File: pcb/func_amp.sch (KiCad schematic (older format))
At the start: 17 parts

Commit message: init pcb layout and gerber
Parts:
- removed J?: PWR, symbol Connector_Generic:Conn_01x02
- added C1: 0.33u, Capacitor_THT:CP_Radial_D5.0mm_P2.50mm, symbol Device:CP
- added C12: 2.2n, Capacitor_THT:C_Rect_L7.0mm_W3.5mm_P5.00mm, symbol Device:C
- added C2: 2.2u, Capacitor_THT:CP_Radial_D5.0mm_P2.50mm, symbol Device:CP
- added C3: 0.1u, Capacitor_THT:CP_Radial_D5.0mm_P2.50mm, symbol Device:CP
- added C4: 1u, Capacitor_THT:CP_Radial_D5.0mm_P2.50mm, symbol Device:CP
- added D1, D2: 1N4001, Diode_THT:D_DO-41_SOD81_P10.16mm_Horizontal, symbol Diode:1N4001
- added J1: PWR, TerminalBlock_Phoenix:TerminalBlock_Phoenix_MKDS-1,5-3-5.08_1x03_P5.08mm_Horizontal, symbol Connector_Generic:Conn_01x03
- added R5: 3R2, Resistor_THT:R_Axial_DIN0207_L6.3mm_D2.5mm_P10.16mm_Horizontal, symbol Device:R
- added R6: 50R, Resistor_THT:R_Axial_DIN0207_L6.3mm_D2.5mm_P10.16mm_Horizontal, symbol Device:R
- added U1: L7815, Package_TO_SOT_THT:TO-220-3_Vertical, symbol Regulator_Linear:L7815
- added U2: L7915, Package_TO_SOT_THT:TO-220-3_Vertical, symbol Regulator_Linear:L7915
- C10, C9: renamed from C?; footprint (none) -> Capacitor_THT:C_Rect_L7.0mm_W3.5mm_P5.00mm
- C11: renamed from C?; footprint (none) -> Capacitor_THT:C_Rect_L10.3mm_W5.7mm_P7.50mm_MKS4
- C5, C6: renamed from C?; footprint (none) -> Capacitor_THT:CP_Radial_D5.0mm_P2.50mm
- C7, C8: renamed from C?; footprint (none) -> Capacitor_THT:CP_Radial_D6.3mm_P2.50mm
- J2: renamed from J?; footprint (none) -> Connector_Coaxial:BNC_TEConnectivity_1478204_Vertical
- J3: renamed from J?; footprint (none) -> TerminalBlock_Phoenix:TerminalBlock_Phoenix_MKDS-1,5-2-5.08_1x02_P5.08mm_Horizontal
- R1, R3: renamed from R?; footprint (none) -> Resistor_THT:R_Axial_DIN0207_L6.3mm_D2.5mm_P10.16mm_Horizontal
- R2: renamed from R?; value 680 -> 680R; footprint (none) -> Resistor_THT:R_Axial_DIN0207_L6.3mm_D2.5mm_P10.16mm_Horizontal
- R4: renamed from R?; value 1 -> 1R; footprint (none) -> Resistor_THT:R_Axial_DIN0207_L6.3mm_D2.5mm_P10.16mm_Horizontal
- gave numbers to parts that had none: 3
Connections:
- net labels added: +15V, +V, -15V, -V
- net labels removed: +12V, -12V
- wire segments 49 -> 87

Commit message: update with available component value
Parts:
- R5: value 3R2 -> 4R7
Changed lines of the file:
@@
 P 5600 3850
 F 0 "R5" V 5680 3850 50  0000 C CNN
-F 1 "3R2" V 5600 3850 50  0000 C CNN
+F 1 "4R7" V 5600 3850 50  0000 C CNN
 F 2 "Resistor_THT:R_Axial_DIN0207_L6.3mm_D2.5mm_P10.16mm_Horizontal" V 5530 3850 50  0001 C CNN
 F 3 "~" H 5600 3850 50  0001 C CNN

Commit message: update schema
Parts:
- removed C12: 2.2n, Capacitor_THT:C_Rect_L7.0mm_W3.5mm_P5.00mm, symbol Device:C
- removed D1, D2: 1N4001, Diode_THT:D_DO-41_SOD81_P10.16mm_Horizontal, symbol Diode:1N4001
- removed J1: PWR, TerminalBlock_Phoenix:TerminalBlock_Phoenix_MKDS-1,5-3-5.08_1x03_P5.08mm_Horizontal, symbol Connector_Generic:Conn_01x03
- removed R5: 4R7, Resistor_THT:R_Axial_DIN0207_L6.3mm_D2.5mm_P10.16mm_Horizontal, symbol Device:R
- removed U1: L7815, Package_TO_SOT_THT:TO-220-3_Vertical, symbol Regulator_Linear:L7815
- removed U2: L7915, Package_TO_SOT_THT:TO-220-3_Vertical, symbol Regulator_Linear:L7915
- added C19: 220pF, symbol Device:C
- added D1: KBP10G, Diode_THT:Diode_Bridge_Vishay_KBPM, symbol Device:D_Bridge_+AA-
- added NT1: Net-Tie_3_Tee, NetTie:NetTie-3_SMD_Pad2.0mm, symbol Device:Net-Tie_3_Tee
- added P1: AC-01B, TerminalBlock_Phoenix:TerminalBlock_Phoenix_MKDS-1,5-3-5.08_1x03_P5.08mm_Horizontal, symbol Connector:Conn_WallPlug_Earth
- added R11, R12: 1k, Resistor_THT:R_Axial_DIN0207_L6.3mm_D2.5mm_P10.16mm_Horizontal, symbol Device:R
- added R7, R8: 5k2, Resistor_THT:R_Axial_DIN0207_L6.3mm_D2.5mm_P10.16mm_Horizontal, symbol Device:R
- added T1: ST-6-20, pl_Transformer:ST-6-20, symbol pl_xformer:ST-6-20
- C1: value 0.33u -> 3300uF; footprint Capacitor_THT:CP_Radial_D5.0mm_P2.50mm -> Capacitor_THT:CP_Radial_D18.0mm_P7.50mm
- C11: footprint Capacitor_THT:C_Rect_L10.3mm_W5.7mm_P7.50mm_MKS4 -> (none)
- C2: value 2.2u -> 3300uF; footprint Capacitor_THT:CP_Radial_D5.0mm_P2.50mm -> Capacitor_THT:CP_Radial_D18.0mm_P7.50mm
- C3: value 0.1u -> 3300uF; footprint Capacitor_THT:CP_Radial_D5.0mm_P2.50mm -> Capacitor_THT:CP_Radial_D18.0mm_P7.50mm
- C4: value 1u -> 3300uF; footprint Capacitor_THT:CP_Radial_D5.0mm_P2.50mm -> Capacitor_THT:CP_Radial_D18.0mm_P7.50mm
- C5: value 1u -> 2.2u; footprint Capacitor_THT:CP_Radial_D5.0mm_P2.50mm -> (none); symbol Device:CP -> Device:C
- C6: value 22u -> 220u; footprint Capacitor_THT:CP_Radial_D5.0mm_P2.50mm -> (none)
- R1: value 22k -> 21k
- R2: value 680R -> 1k
- R4: value 1R -> 10R; footprint Resistor_THT:R_Axial_DIN0207_L6.3mm_D2.5mm_P10.16mm_Horizontal -> (none)
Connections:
- net labels added: GNDPWR, GNDS, L, N
- net labels removed: +15V, -15V
- wire segments 87 -> 102
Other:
- note added: "115VAC 60Hz Primary\n20VAC 20VA Secondary"
- note added: "50Ohm Input"
- note added: "Amplifier"
- note added: "Linear Power Supply"
- note added: "Power Entry Module with\nSwitch and Fuse"
- note added: "Star Ground"
- note added: "size discharge resistors so \nno load votlage does not \nexceeded tda2030 Vmax"
- moved on the sheet: C10, C11, C6, C7, C8, C9, D3, D4, J2, J3, R1, R2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

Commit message: update footprints
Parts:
- added H1, H2, H3, H4: MountingHole, MountingHole:MountingHole_3.2mm_M3, symbol Mechanical:MountingHole
- C10, C9: footprint Capacitor_THT:C_Rect_L7.0mm_W3.5mm_P5.00mm -> Capacitor_THT:C_Rect_L13.0mm_W4.0mm_P10.00mm_FKS3_FKP3_MKS4
- C11: footprint (none) -> Capacitor_THT:C_Rect_L13.0mm_W8.0mm_P10.00mm_FKS3_FKP3_MKS4
- C19: value 220pF -> 220p; footprint (none) -> Capacitor_THT:C_Rect_L7.2mm_W4.5mm_P5.00mm_FKS2_FKP2_MKS2_MKP2
- C5: footprint (none) -> Capacitor_THT:C_Rect_L31.5mm_W11.0mm_P27.50mm_MKS4
- C6: footprint (none) -> Capacitor_THT:CP_Radial_D8.0mm_P3.80mm
- C7, C8: footprint Capacitor_THT:CP_Radial_D6.3mm_P2.50mm -> Capacitor_THT:CP_Radial_D8.0mm_P3.80mm
- J2: footprint Connector_Coaxial:BNC_TEConnectivity_1478204_Vertical -> Connector_Coaxial:BNC_Amphenol_B6252HB-NPP3G-50_Horizontal
- R4: footprint (none) -> Resistor_THT:R_Axial_DIN0411_L9.9mm_D3.6mm_P15.24mm_Horizontal
- T1: symbol pl_xformer:ST-6-20 -> pl_xformer:Signal_Transfromer_ST_Series
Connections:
- net GNDPWR: now also NT1.3; no longer NT1.1
- net GNDS: now also NT1.1; no longer NT1.3
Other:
- note added: "ERC Happy Zone"
- note added: "Mounting Holes"
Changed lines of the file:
@@
 F 0 "C7" H 4125 2800 50  0000 L CNN
 F 1 "100u" H 4125 2600 50  0000 L CNN
-F 2 "Capacitor_THT:CP_Radial_D6.3mm_P2.50mm" H 4138 2550 50  0001 C CNN
+F 2 "Capacitor_THT:CP_Radial_D8.0mm_P3.80mm" H 4138 2550 50  0001 C CNN
 F 3 "~" H 4100 2700 50  0001 C CNN
 	1    4100 2700
@@
 F 0 "C6" H 3825 4750 50  0000 L CNN
 F 1 "220u" H 3825 4550 50  0000 L CNN
-F 2 "" H 3838 4500 50  0001 C CNN
+F 2 "Capacitor_THT:CP_Radial_D8.0mm_P3.80mm" H 3838 4500 50  0001 C CNN
 F 3 "~" H 3800 4650 50  0001 C CNN
 	1    3800 4650
@@
 F 0 "C9" H 4625 2800 50  0000 L CNN
 F 1 "100n" H 4625 2600 50  0000 L CNN
-F 2 "Capacitor_THT:C_Rect_L7.0mm_W3.5mm_P5.00mm" H 4638 2550 50  0001 C CNN
+F 2 "Capacitor_THT:C_Rect_L13.0mm_W4.0mm_P10.00mm_FKS3_FKP3_MKS4" H 4638 2550 50  0001 C CNN
 F 3 "~" H 4600 2700 50  0001 C CNN
 	1    4600 2700
@@
 F 0 "C11" H 5475 4750 50  0000 L CNN
 F 1 "220n" H 5475 4550 50  0000 L CNN
-F 2 "" H 5488 4500 50  0001 C CNN
+F 2 "Capacitor_THT:C_Rect_L13.0mm_W8.0mm_P10.00mm_FKS3_FKP3_MKS4" H 5488 4500 50  0001 C CNN
 F 3 "~" H 5450 4650 50  0001 C CNN
 	1    5450 4650
@@
 F 0 "J2" H 1760 3670 50  0000 C CNN
 F 1 "IN" V 1865 3550 50  0000 C CNN
-F 2 "Connector_Coaxial:BNC_TEConnectivity_1478204_Vertical" H 1750 3550 50  0001 C CNN
+F 2 "Connector_Coaxial:BNC_Amphenol_B6252HB-NPP3G-50_Horizontal" H 1750 3550 50  0001 C CNN
 F 3 " ~" H 1750 3550 50  0001 C CNN
 	1    1750 3550
@@
 F 0 "C10" H 4625 4750 50  0000 L CNN
 F 1 "100n" H 4625 4550 50  0000 L CNN
-F 2 "Capacitor_THT:C_Rect_L7.0mm_W3.5mm_P5.00mm" H 4638 4500 50  0001 C CNN
+F 2 "Capacitor_THT:C_Rect_L13.0mm_W4.0mm_P10.00mm_FKS3_FKP3_MKS4" H 4638 4500 50  0001 C CNN
 F 3 "~" H 4600 4650 50  0001 C CNN
 	1    4600 4650
@@
 F 0 "C8" H 4125 4750 50  0000 L CNN
 F 1 "100u" H 4125 4550 50  0000 L CNN
-F 2 "Capacitor_THT:CP_Radial_D6.3mm_P2.50mm" H 4138 4500 50  0001 C CNN
+F 2 "Capacitor_THT:CP_Radial_D8.0mm_P3.80mm" H 4138 4500 50  0001 C CNN
 F 3 "~" H 4100 4650 50  0001 C CNN
 	1    4100 4650
@@
 F 0 "R4" V 5530 4200 50  0000 C CNN
 F 1 "10R" V 5450 4200 50  0000 C CNN
-F 2 "" V 5380 4200 50  0001 C CNN
+F 2 "Resistor_THT:R_Axial_DIN0411_L9.9mm_D3.6mm_P15.24mm_Horizontal" V 5380 4200 50  0001 C CNN
 F 3 "~" H 5450 4200 50  0001 C CNN
 	1    5450 4200
@@
 $EndComp
 $Comp
-L pl_xformer:ST-6-20 T1
+L pl_xformer:Signal_Transfromer_ST_Series T1
 U 1 1 61ACFFF1
 P 2200 1400
@@
 F 0 "C5" H 2375 3650 50  0000 L CNN
 F 1 "2.2u" H 2375 3450 50  0000 L CNN
-F 2 "" H 2388 3400 50  0001 C CNN
+F 2 "Capacitor_THT:C_Rect_L31.5mm_W11.0mm_P27.50mm_MKS4" H 2388 3400 50  0001 C CNN
 F 3 "~" H 2350 3550 50  0001 C CNN
 	1    2350 3550
@@
 P 3500 4300
 F 0 "C19" H 3525 4400 50  0000 L CNN
-F 1 "220pF" H 3525 4200 50  0000 L CNN
-F 2 "" H 3538 4150 50  0001 C CNN
+F 1 "220p" H 3525 4200 50  0000 L CNN
+F 2 "Capacitor_THT:C_Rect_L7.2mm_W4.5mm_P5.00mm_FKS2_FKP2_MKS2_MKP2" H 3538 4150 50  0001 C CNN
 F 3 "~" H 3500 4300 50  0001 C CNN
 	1    3500 4300
@@
 L power:GNDPWR #PWR017
 U 1 1 61EDE077
-P 6450 2700
-F 0 "#PWR017" H 6450 2500 50  0001 C CNN
-F 1 "GNDPWR" H 6450 2570 50  0000 C CNN
-F 2 "" H 6450 2650 50  0001 C CNN
-F 3 "" H 6450 2650 50  0001 C CNN
-	1    6450 2700
+P 6850 2700
+F 0 "#PWR017" H 6850 2500 50  0001 C CNN
+F 1 "GNDPWR" H 6850 2570 50  0000 C CNN
+F 2 "" H 6850 2650 50  0001 C CNN
+F 3 "" H 6850 2650 50  0001 C CNN
+	1    6850 2700
 	1    0    0    -1
 $EndComp
@@
 L power:GNDS #PWR018
 U 1 1 61EDE60D
-P 6850 2700
-F 0 "#PWR018" H 6850 2450 50  0001 C CNN
-F 1 "GNDS" H 6850 2550 50  0000 C CNN
-F 2 "" H 6850 2700 50  0001 C CNN
-F 3 "" H 6850 2700 50  0001 C CNN
-	1    6850 2700
+P 6450 2700
+F 0 "#PWR018" H 6450 2450 50  0001 C CNN
+F 1 "GNDS" H 6450 2550 50  0000 C CNN
+F 2 "" H 6450 2700 50  0001 C CNN
+F 3 "" H 6450 2700 50  0001 C CNN
+	1    6450 2700
 	1    0    0    -1
 $EndComp
@@
 Wire Notes Line
 	7350 2200 7350 2900
+$Comp
+L Mechanical:MountingHole H1
+U 1 1 61B1CEBF
+P 2200 6150
+F 0 "H1" H 2200 6350 50  0000 C CNN
+F 1 "MountingHole" H 2200 6275 50  0000 C CNN
+F 2 "MountingHole:MountingHole_3.2mm_M3" H 2200 6150 50  0001 C CNN
+F 3 "~" H 2200 6150 50  0001 C CNN
+	1    2200 6150
+	1    0    0    -1
+$EndComp
+$Comp
+L Mechanical:MountingHole H3
+U 1 1 61B1DBA5
+P 2750 6150
+F 0 "H3" H 2750 6350 50  0000 C CNN
+F 1 "MountingHole" H 2750 6275 50  0000 C CNN
+F 2 "MountingHole:MountingHole_3.2mm_M3" H 2750 6150 50  0001 C CNN
+F 3 "~" H 2750 6150 50  0001 C CNN
+	1    2750 6150
+	1    0    0    -1
+$EndComp
+$Comp
+L Mechanical:MountingHole H4
+U 1 1 61B1DED8
+P 2750 6500
+F 0 "H4" H 2750 6700 50  0000 C CNN
+F 1 "MountingHole" H 2750 6625 50  0000 C CNN
+F 2 "MountingHole:MountingHole_3.2mm_M3" H 2750 6500 50  0001 C CNN
+F 3 "~" H 2750 6500 50  0001 C CNN
+	1    2750 6500
+	1    0    0    -1
+$EndComp
+$Comp
+L Mechanical:MountingHole H2
+U 1 1 61B1E1A3
+P 2200 6500
+F 0 "H2" H 2200 6700 50  0000 C CNN
+F 1 "MountingHole" H 2200 6625 50  0000 C CNN
+F 2 "MountingHole:MountingHole_3.2mm_M3" H 2200 6500 50  0001 C CNN
+F 3 "~" H 2200 6500 50  0001 C CNN
+	1    2200 6500
+	1    0    0    -1
+$EndComp
+$Comp
+L pl_power:-V #PWR?
+U 1 1 61B200D1
+P 800 7150
+F 0 "#PWR?" H 800 7000 50  0001 C CNN
+F 1 "-V" H 800 7290 50  0000 C CNN
+F 2 "" H 800 7150 50  0001 C CNN
+F 3 "" H 800 7150 50  0001 C CNN
+	1    800  7150
+	-1   0    0    1
+$EndComp
+$Comp
+L pl_power:+V #PWR?
+U 1 1 61B21460
+P 1200 7150
+F 0 "#PWR?" H 1200 7000 50  0001 C CNN
+F 1 "+V" H 1200 7290 50  0000 C CNN
+F 2 "" H 1200 7150 50  0001 C CNN
+F 3 "" H 1200 7150 50  0001 C CNN
+	1    1200 7150
+	-1   0    0    1
+$EndComp
+$Comp
+L power:GNDPWR #PWR?
+U 1 1 61B219D2
+P 1600 7150
+F 0 "#PWR?" H 1600 6950 50  0001 C CNN
+F 1 "GNDPWR" H 1600 7020 50  0000 C CNN
+F 2 "" H 1600 7100 50  0001 C CNN
+F 3 "" H 1600 7100 50  0001 C CNN
+	1    1600 7150
+	1    0    0    -1
+$EndComp
+$Comp
+L power:GNDS #PWR?
+U 1 1 61B2230A
+P 1000 7700
+F 0 "#PWR?" H 1000 7450 50  0001 C CNN
+F 1 "GNDS" H 1000 7550 50  0000 C CNN
+F 2 "" H 1000 7700 50  0001 C CNN
+F 3 "" H 1000 7700 50  0001 C CNN
+	1    1000 7700
+	1    0    0    -1
+$EndComp
+$Comp
+L power:GND #PWR?
+U 1 1 61B227D9
+P 1400 7700
+F 0 "#PWR?" H 1400 7450 50  0001 C CNN
+F 1 "GND" H 1400 7550 50  0000 C CNN
+F 2 "" H 1400 7700 50  0001 C CNN
+F 3 "" H 1400 7700 50  0001 C CNN
+	1    1400 7700
+	1    0    0    -1
+$EndComp
+$Comp
+L power:PWR_FLAG #FLG?
+U 1 1 61B23F6E
+P 800 7050
+F 0 "#FLG?" H 800 7125 50  0001 C CNN
+F 1 "PWR_FLAG" H 800 7200 50  0000 C CNN
+F 2 "" H 800 7050 50  0001 C CNN
+F 3 "~" H 800 7050 50  0001 C CNN
+	1    800  7050
+	1    0    0    -1
+$EndComp
+$Comp
+L power:PWR_FLAG #FLG?
+U 1 1 61B2479D
+P 1200 7050
+F 0 "#FLG?" H 1200 7125 50  0001 C CNN
+F 1 "PWR_FLAG" H 1200 7200 50  0000 C CNN
+F 2 "" H 1200 7050 50  0001 C CNN
+F 3 "~" H 1200 7050 50  0001 C CNN
+	1    1200 7050
+	1    0    0    -1
+$EndComp
+Wire Wire Line
+	1200 7050 1200 7150
+Wire Wire Line
+	800  7050 800  7150
+$Comp
+L power:PWR_FLAG #FLG?
+U 1 1 61B34C34
+P 1600 7050
+F 0 "#FLG?" H 1600 7125 50  0001 C CNN
+F 1 "PWR_FLAG" H 1600 7200 50  0000 C CNN
+F 2 "" H 1600 7050 50  0001 C CNN
+F 3 "~" H 1600 7050 50  0001 C CNN
+	1    1600 7050
+	1    0    0    -1
+$EndComp
+$Comp
+L power:PWR_FLAG #FLG?
+U 1 1 61B34F7D
+P 1000 7600
+F 0 "#FLG?" H 1000 7675 50  0001 C CNN
+F 1 "PWR_FLAG" H 1000 7750 50  0000 C CNN
+F 2 "" H 1000 7600 50  0001 C CNN
+F 3 "~" H 1000 7600 50  0001 C CNN
+	1    1000 7600
+	1    0    0    -1
+$EndComp
+$Comp
+L power:PWR_FLAG #FLG?
+U 1 1 61B3526D
+P 1400 7600
+F 0 "#FLG?" H 1400 7675 50  0001 C CNN
+F 1 "PWR_FLAG" H 1400 7750 50  0000 C CNN
+F 2 "" H 1400 7600 50  0001 C CNN
+F 3 "~" H 1400 7600 50  0001 C CNN
+	1    1400 7600
+	1    0    0    -1
+$EndComp
+Wire Wire Line
+	1400 7600 1400 7700
+Wire Wire Line
+	1000 7600 1000 7700
+Wire Wire Line
+	1600 7050 1600 7150
+Text Notes 550  6800 0    50   ~ 0
+ERC Happy Zone
+Wire Notes Line
+	550  6800 1850 6800
+Wire Notes Line
+	1850 7950 550  7950
+Wire Notes Line
+	550  7950 550  6700
+Wire Notes Line
+	550  6700 1850 6700
+Wire Notes Line
+	1850 6700 1850 7950
+Text Notes 1900 5850 0    50   ~ 0
+Mounting Holes
+Wire Notes Line
+	1900 5850 3050 5850
+Wire Notes Line
+	3050 6650 1900 6650
+Wire Notes Line
+	1900 6650 1900 5750
+Wire Notes Line
+	1900 5750 3050 5750
+Wire Notes Line
+	3050 5750 3050 6650
 $EndSCHEMATC

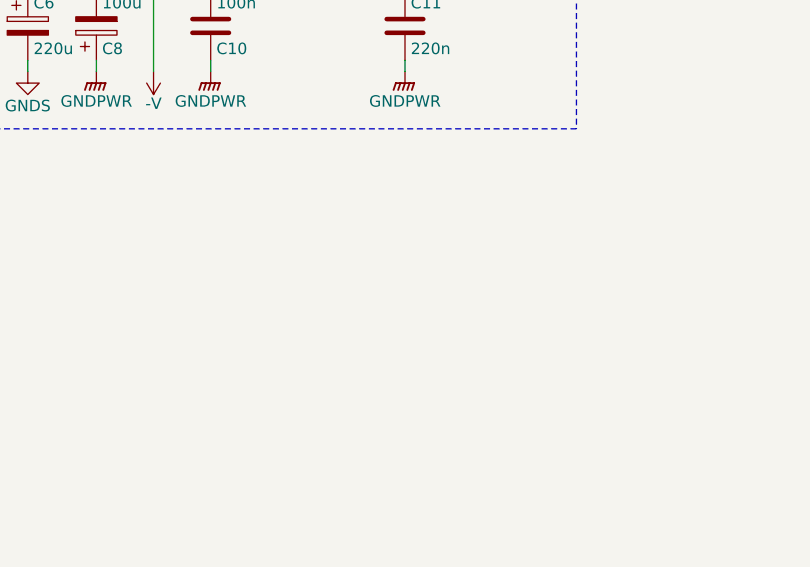
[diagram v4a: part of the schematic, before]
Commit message: add heatsink
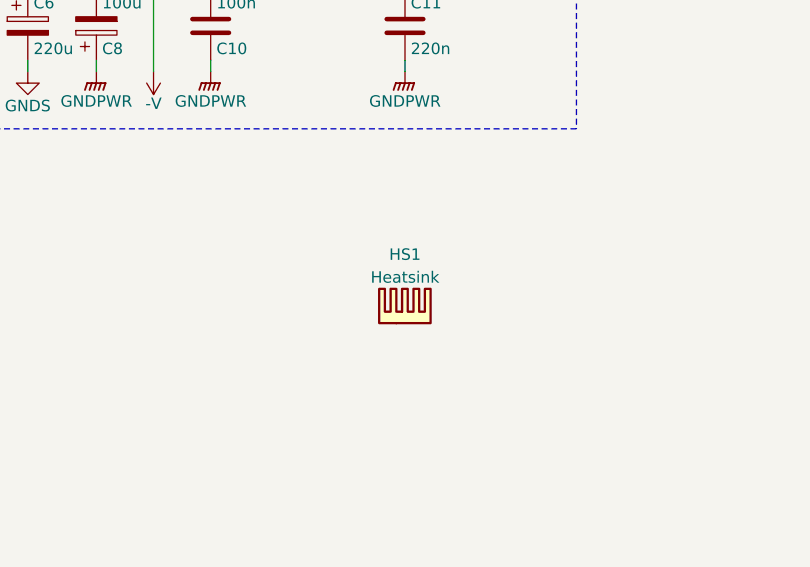
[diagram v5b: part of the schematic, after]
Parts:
- added HS1: Heatsink, pl_heatsink:random_psu_heatsink, symbol Mechanical:Heatsink
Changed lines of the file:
@@
 $EndComp
 $Comp
-L pl_power:-V #PWR?
+L pl_power:-V #PWR0101
 U 1 1 61B200D1
 P 800 7150
-F 0 "#PWR?" H 800 7000 50  0001 C CNN
+F 0 "#PWR0101" H 800 7000 50  0001 C CNN
 F 1 "-V" H 800 7290 50  0000 C CNN
 F 2 "" H 800 7150 50  0001 C CNN
@@
 $EndComp
 $Comp
-L pl_power:+V #PWR?
+L pl_power:+V #PWR0102
 U 1 1 61B21460
 P 1200 7150
-F 0 "#PWR?" H 1200 7000 50  0001 C CNN
+F 0 "#PWR0102" H 1200 7000 50  0001 C CNN
 F 1 "+V" H 1200 7290 50  0000 C CNN
 F 2 "" H 1200 7150 50  0001 C CNN
@@
 $EndComp
 $Comp
-L power:GNDPWR #PWR?
+L power:GNDPWR #PWR0103
 U 1 1 61B219D2
 P 1600 7150
-F 0 "#PWR?" H 1600 6950 50  0001 C CNN
+F 0 "#PWR0103" H 1600 6950 50  0001 C CNN
 F 1 "GNDPWR" H 1600 7020 50  0000 C CNN
 F 2 "" H 1600 7100 50  0001 C CNN
@@
 $EndComp
 $Comp
-L power:GNDS #PWR?
+L power:GNDS #PWR0104
 U 1 1 61B2230A
 P 1000 7700
-F 0 "#PWR?" H 1000 7450 50  0001 C CNN
+F 0 "#PWR0104" H 1000 7450 50  0001 C CNN
 F 1 "GNDS" H 1000 7550 50  0000 C CNN
 F 2 "" H 1000 7700 50  0001 C CNN
@@
 $EndComp
 $Comp
-L power:GND #PWR?
+L power:GND #PWR0105
 U 1 1 61B227D9
 P 1400 7700
-F 0 "#PWR?" H 1400 7450 50  0001 C CNN
+F 0 "#PWR0105" H 1400 7450 50  0001 C CNN
 F 1 "GND" H 1400 7550 50  0000 C CNN
 F 2 "" H 1400 7700 50  0001 C CNN
@@
 $EndComp
 $Comp
-L power:PWR_FLAG #FLG?
+L power:PWR_FLAG #FLG0101
 U 1 1 61B23F6E
 P 800 7050
-F 0 "#FLG?" H 800 7125 50  0001 C CNN
+F 0 "#FLG0101" H 800 7125 50  0001 C CNN
 F 1 "PWR_FLAG" H 800 7200 50  0000 C CNN
 F 2 "" H 800 7050 50  0001 C CNN
@@
 $EndComp
 $Comp
-L power:PWR_FLAG #FLG?
+L power:PWR_FLAG #FLG0102
 U 1 1 61B2479D
 P 1200 7050
-F 0 "#FLG?" H 1200 7125 50  0001 C CNN
+F 0 "#FLG0102" H 1200 7125 50  0001 C CNN
 F 1 "PWR_FLAG" H 1200 7200 50  0000 C CNN
 F 2 "" H 1200 7050 50  0001 C CNN
@@
 	800  7050 800  7150
 $Comp
-L power:PWR_FLAG #FLG?
+L power:PWR_FLAG #FLG0103
 U 1 1 61B34C34
 P 1600 7050
-F 0 "#FLG?" H 1600 7125 50  0001 C CNN
+F 0 "#FLG0103" H 1600 7125 50  0001 C CNN
 F 1 "PWR_FLAG" H 1600 7200 50  0000 C CNN
 F 2 "" H 1600 7050 50  0001 C CNN
@@
 $EndComp
 $Comp
-L power:PWR_FLAG #FLG?
+L power:PWR_FLAG #FLG0104
 U 1 1 61B34F7D
 P 1000 7600
-F 0 "#FLG?" H 1000 7675 50  0001 C CNN
+F 0 "#FLG0104" H 1000 7675 50  0001 C CNN
 F 1 "PWR_FLAG" H 1000 7750 50  0000 C CNN
 F 2 "" H 1000 7600 50  0001 C CNN
@@
 $EndComp
 $Comp
-L power:PWR_FLAG #FLG?
+L power:PWR_FLAG #FLG0105
 U 1 1 61B3526D
 P 1400 7600
-F 0 "#FLG?" H 1400 7675 50  0001 C CNN
+F 0 "#FLG0105" H 1400 7675 50  0001 C CNN
 F 1 "PWR_FLAG" H 1400 7750 50  0000 C CNN
 F 2 "" H 1400 7600 50  0001 C CNN
@@
 Wire Notes Line
 	3050 5750 3050 6650
+$Comp
+L Mechanical:Heatsink HS1
+U 1 1 61BCD7D7
+P 5450 5950
+F 0 "HS1" H 5450 6250 50  0000 C CNN
+F 1 "Heatsink" H 5450 6150 50  0000 C CNN
+F 2 "pl_heatsink:random_psu_heatsink" H 5462 5900 50  0001 C CNN
+F 3 "~" H 5462 5900 50  0001 C CNN
+	1    5450 5950
+	1    0    0    -1
+$EndComp
 $EndSCHEMATC

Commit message: spade grounds for star ground
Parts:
- removed J2: IN, Connector_Coaxial:BNC_Amphenol_B6252HB-NPP3G-50_Horizontal, symbol Connector:Conn_Coaxial
- removed J3: LOAD, TerminalBlock_Phoenix:TerminalBlock_Phoenix_MKDS-1,5-2-5.08_1x02_P5.08mm_Horizontal, symbol Connector_Generic:Conn_01x02
- removed NT1: Net-Tie_3_Tee, NetTie:NetTie-3_SMD_Pad2.0mm, symbol Device:Net-Tie_3_Tee
- removed P1: AC-01B, TerminalBlock_Phoenix:TerminalBlock_Phoenix_MKDS-1,5-3-5.08_1x03_P5.08mm_Horizontal, symbol Connector:Conn_WallPlug_Earth
- added J1: L, pl_connector:TE_0.25in_spade_63824-1, symbol Connector:Conn_01x01_Male
- added J10, J5, J8: GNDS, pl_connector:TE_0.25in_spade_63824-1, symbol Connector:Conn_01x01_Male
- added J11, J7, J9: GND, pl_connector:TE_0.25in_spade_63824-1, symbol Connector:Conn_01x01_Male
- added J2: N, pl_connector:TE_0.25in_spade_63824-1, symbol Connector:Conn_01x01_Male
- added J3: G, pl_connector:TE_0.25in_spade_63824-1, symbol Connector:Conn_01x01_Male
- added J4: IN, pl_connector:TE_0.25in_spade_63824-1, symbol Connector:Conn_01x01_Male
- added J6: OUT, pl_connector:TE_0.25in_spade_63824-1, symbol Connector:Conn_01x01_Male
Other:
- note added: "Wire from GND"
- note added: "Wire from GNDS"
- note added: "Wire to GRDPWR"
- note removed: "Star Ground"
- moved on the sheet: HS1
